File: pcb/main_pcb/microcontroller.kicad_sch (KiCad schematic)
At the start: 20 parts

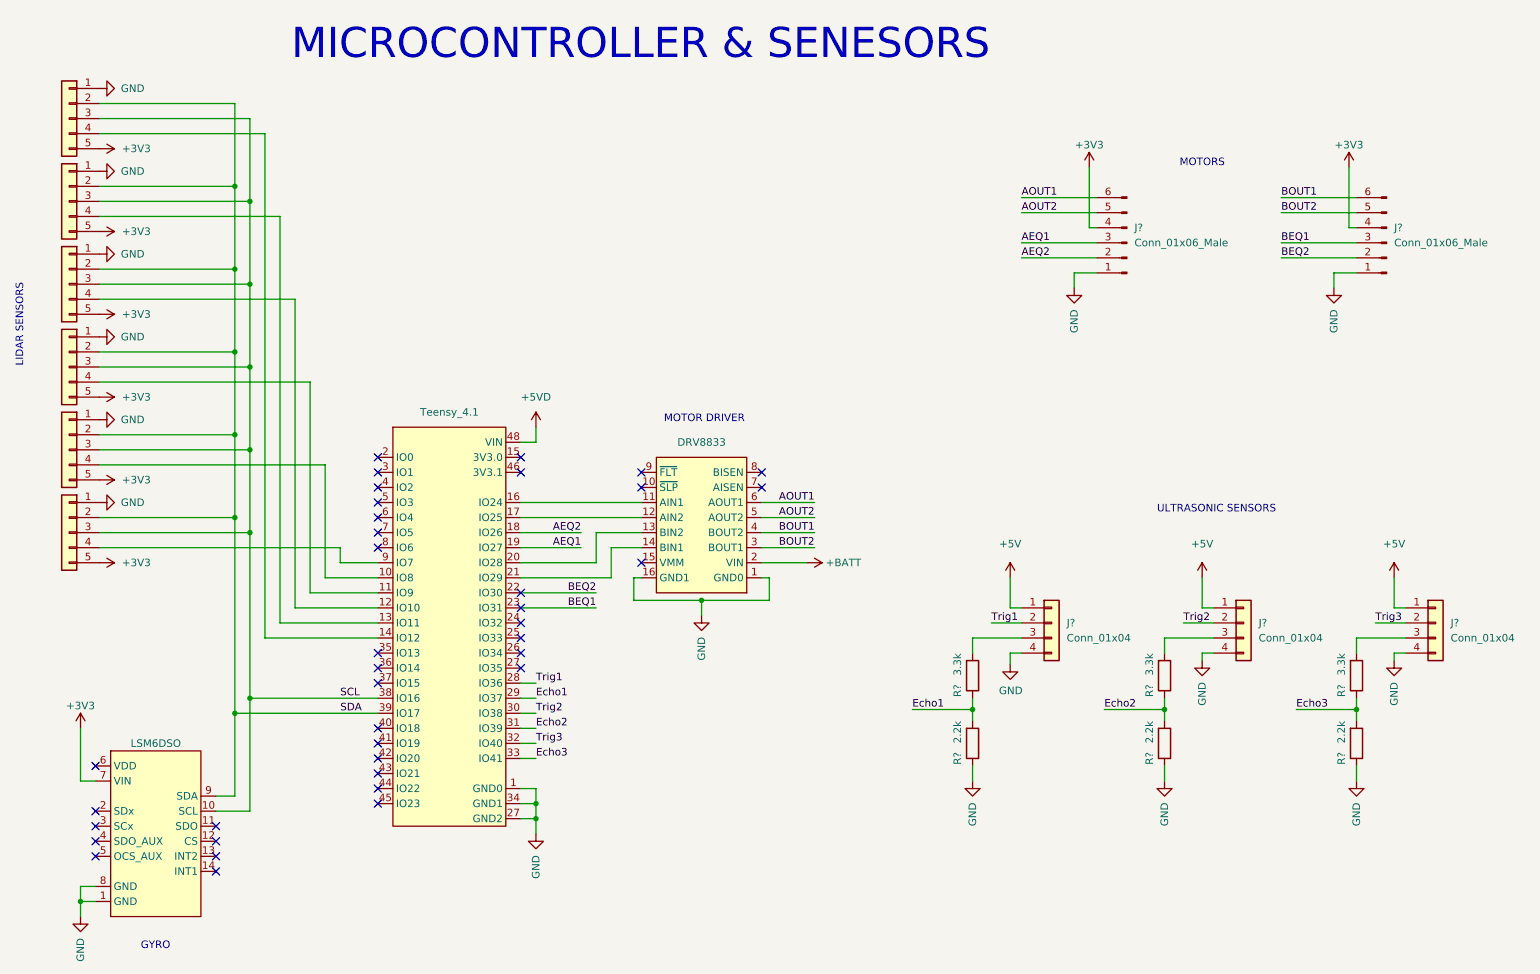
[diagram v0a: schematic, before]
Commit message: Annotate & begin footprint assignment
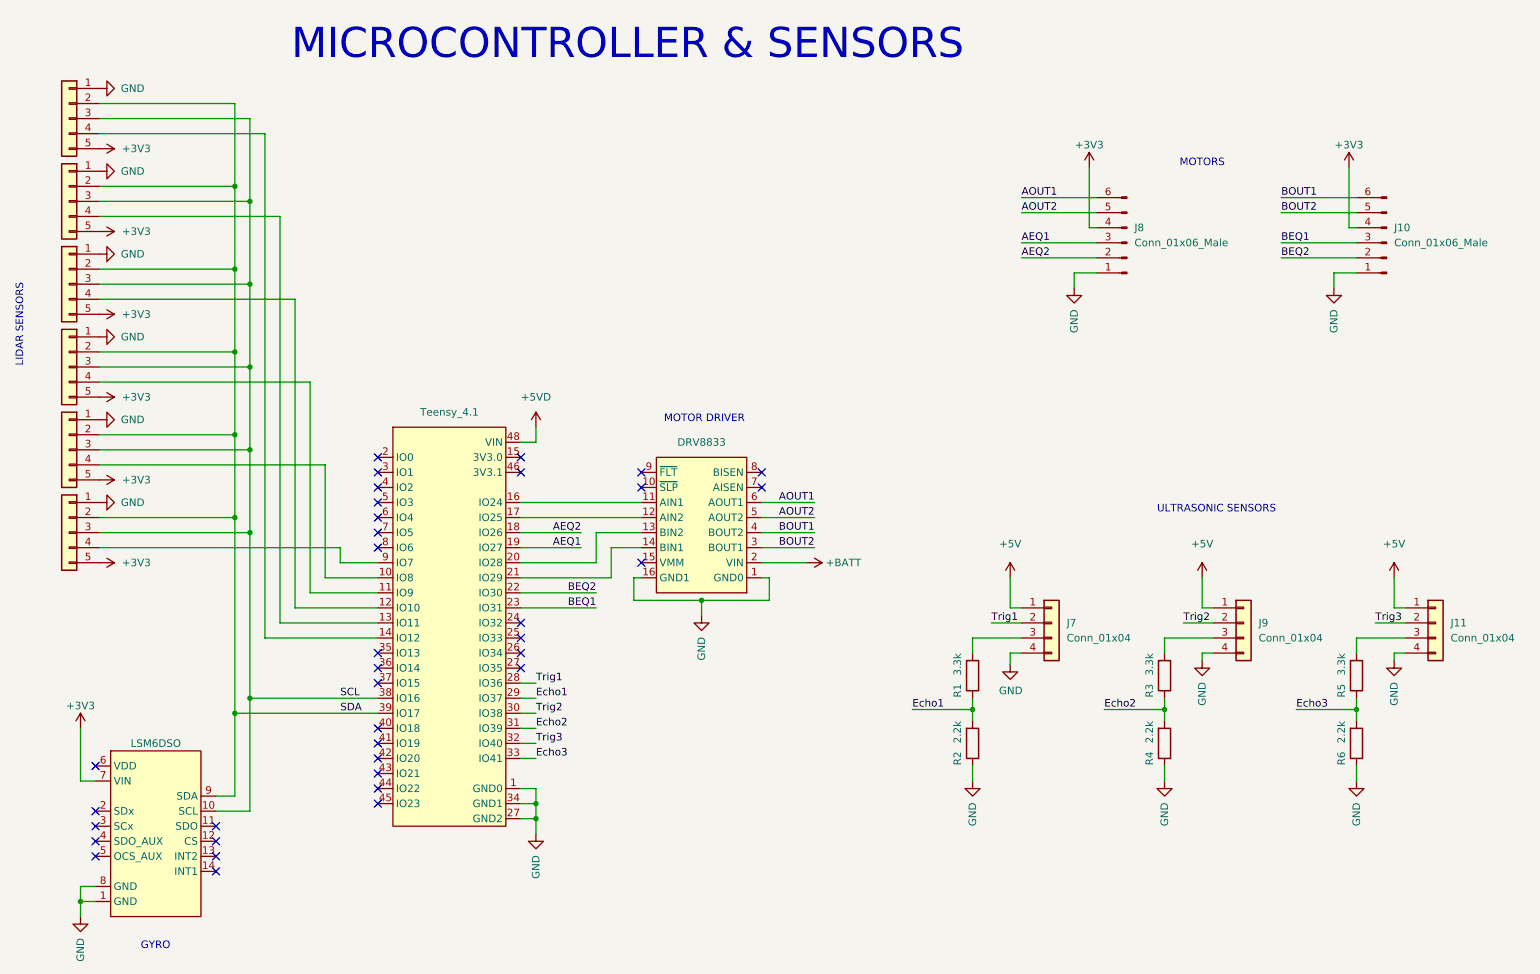
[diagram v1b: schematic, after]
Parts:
- removed J? (x5): Conn_01x04, symbol Connector_Generic:Conn_01x05
- added J2, J3, J4, J5, J6: Conn_01x05, Connector_JST:JST_XH_B5B-XH-A_1x05_P2.50mm_Vertical, symbol Connector_Generic:Conn_01x05
- J1: renamed from J?; value Conn_01x04 -> Conn_01x05; footprint (none) -> Connector_JST:JST_XH_B5B-XH-A_1x05_P2.50mm_Vertical
- J10, J8: renamed from J?; footprint (none) -> Connector_JST:JST_XH_B6B-XH-A_1x06_P2.50mm_Vertical
- J11, J7, J9: renamed from J?; footprint (none) -> Connector_JST:JST_XH_B4B-XH-A_1x04_P2.50mm_Vertical
- R1, R2, R3, R4, R5, R6: renamed from R?; footprint (none) -> Resistor_SMD:R_0603_1608Metric_Pad0.98x0.95mm_HandSolder
- gave numbers to parts that had none: 3
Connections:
- net +3V3: now also J2.5 (Pin_5), J3.5 (Pin_5), J4.5 (Pin_5), J5.5 (Pin_5), J6.5 (Pin_5)
- net GND: now also J2.1 (Pin_1), J3.1 (Pin_1), J4.1 (Pin_1), J5.1 (Pin_1), J6.1 (Pin_1)
- net SCL: now also J2.3 (Pin_3), J3.3 (Pin_3), J4.3 (Pin_3), J5.3 (Pin_3), J6.3 (Pin_3)
- net SDA: now also J2.2 (Pin_2), J3.2 (Pin_2), J4.2 (Pin_2), J5.2 (Pin_2), J6.2 (Pin_2)
- net at U2.10 (IO8): now also J5.4 (Pin_4)
- net at U2.11 (IO9): now also J4.4 (Pin_4)
- net at U2.13 (IO11): now also J2.4 (Pin_4)
- net at U2.12 (IO10): now also J3.4 (Pin_4)
- net at U2.9 (IO7): now also J6.4 (Pin_4)
- no-connect marks 38 -> 36
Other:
- note added: "MICROCONTROLLER & SENSORS"
- note removed: "MICROCONTROLLER & SENESORS"

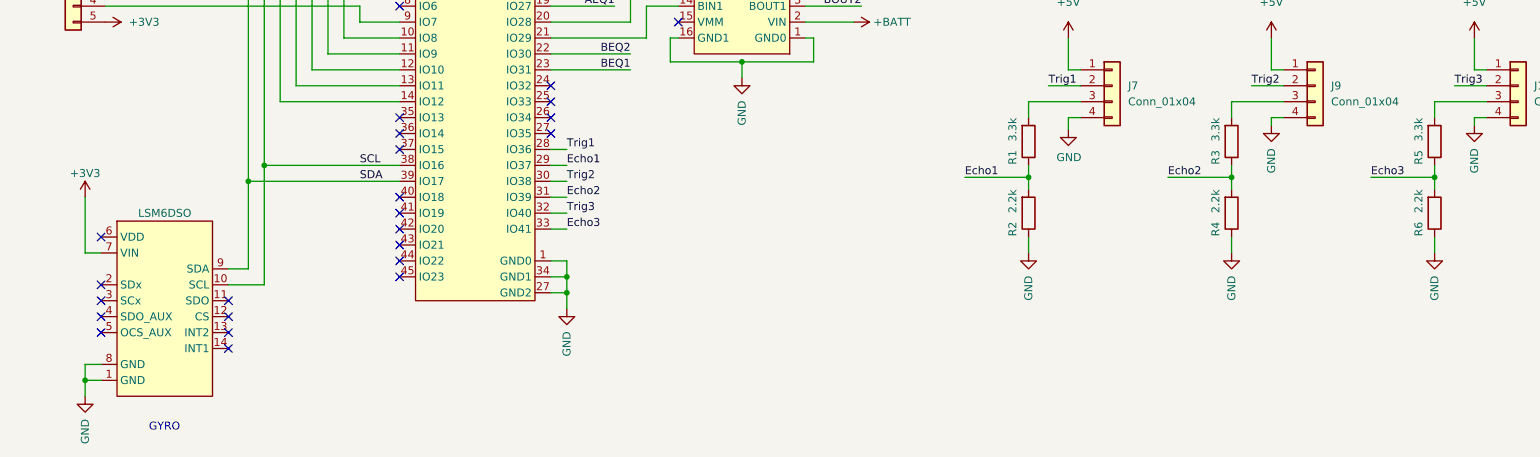
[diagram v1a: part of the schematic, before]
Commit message: Create footprints for carriers; complete footprint assignment
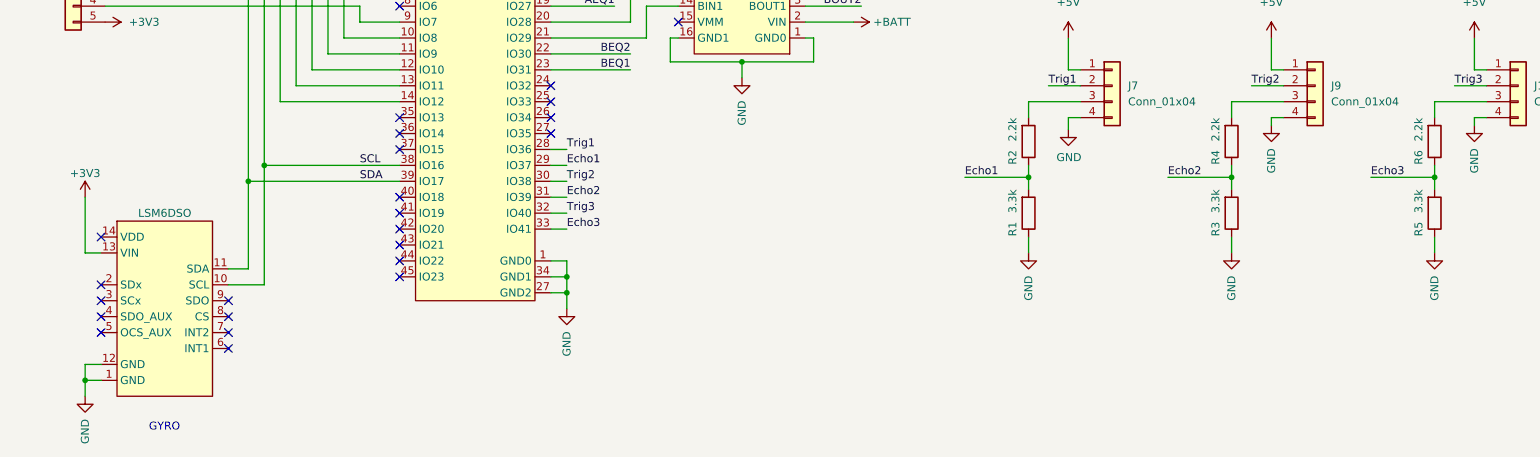
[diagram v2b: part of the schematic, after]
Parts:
- U1: footprint (none) -> custom_footprints:SENS_LSM6DSO_Pololu_2798
- U2: footprint (none) -> custom_footprints:MCU_TEENSY41_PJRC
- U3: footprint (none) -> custom_footprints:DRV_DRV8833_Pololu_2130
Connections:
- net +3V3: now also U1.13 (VIN); no longer U1.7 (VIN)
- net Echo1: now also R1.2, R2.1; no longer R1.1, R2.2
- net Echo2: now also R3.2, R4.1; no longer R3.1, R4.2
- net Echo3: now also R5.2, R6.1; no longer R5.1, R6.2
- net GND: now also R1.1, R3.1, R5.1, U1.12 (GND); no longer R2.1, R4.1, R6.1, U1.8 (GND)
- net SDA: now also U1.11 (SDA); no longer U1.9 (SDA)
- net at J7.3 (Pin_3): now also R2.2; no longer R1.2
- net at J9.3 (Pin_3): now also R4.2; no longer R3.2
- net at J11.3 (Pin_3): now also R6.2; no longer R5.2
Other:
- moved on the sheet: R1, R2, R3, R4, R5, R6
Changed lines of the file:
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@@
     (pin "1")
   )
-  (symbol (lib_id "Device:R") (at 182.88 130.81 0) (mirror x) (unit 1)
-    (in_bom yes) (on_board yes)
-    (property "Reference" "R1" (id 0) (at 180.34 133.35 90))
-    (property "Value" "3.3k" (id 1) (at 180.34 128.905 90))
-    (property "Footprint" "Resistor_SMD:R_0603_1608Metric_Pad0.98x0.95mm_HandSolder" (id 2) (at 181.102 130.81 90)
-      (effects (font (size 1.27 1.27)) hide)
-    )
-    (property "Datasheet" "~" (id 3) (at 182.88 130.81 0)
-      (effects (font (size 1.27 1.27)) hide)
-    )
-    (pin "1")
-    (pin "2")
-  )
-  (symbol (lib_id "Device:R") (at 215.265 130.81 0) (mirror x) (unit 1)
-    (in_bom yes) (on_board yes)
-    (property "Reference" "R3" (id 0) (at 212.725 133.35 90))
-    (property "Value" "3.3k" (id 1) (at 212.725 128.905 90))
-    (property "Footprint" "Resistor_SMD:R_0603_1608Metric_Pad0.98x0.95mm_HandSolder" (id 2) (at 213.487 130.81 90)
-      (effects (font (size 1.27 1.27)) hide)
-    )
-    (property "Datasheet" "~" (id 3) (at 215.265 130.81 0)
+  (symbol (lib_id "Device:R") (at 182.88 142.24 0) (mirror x) (unit 1)
+    (in_bom yes) (on_board yes)
+    (property "Reference" "R1" (id 0) (at 180.34 144.78 90))
+    (property "Value" "3.3k" (id 1) (at 180.34 140.335 90))
+    (property "Footprint" "Resistor_SMD:R_0603_1608Metric_Pad0.98x0.95mm_HandSolder" (id 2) (at 181.102 142.24 90)
+      (effects (font (size 1.27 1.27)) hide)
+    )
+    (property "Datasheet" "~" (id 3) (at 182.88 142.24 0)
+      (effects (font (size 1.27 1.27)) hide)
+    )
+    (pin "1")
+    (pin "2")
+  )
+  (symbol (lib_id "Device:R") (at 215.265 142.24 0) (mirror x) (unit 1)
+    (in_bom yes) (on_board yes)
+    (property "Reference" "R3" (id 0) (at 212.725 144.78 90))
+    (property "Value" "3.3k" (id 1) (at 212.725 140.335 90))
+    (property "Footprint" "Resistor_SMD:R_0603_1608Metric_Pad0.98x0.95mm_HandSolder" (id 2) (at 213.487 142.24 90)
+      (effects (font (size 1.27 1.27)) hide)
+    )
+    (property "Datasheet" "~" (id 3) (at 215.265 142.24 0)
       (effects (font (size 1.27 1.27)) hide)
     )
@@
     )
     (property "Value" "LSM6DSO" (id 1) (at 45.085 142.24 0))
-    (property "Footprint" "" (id 2) (at 41.275 152.4 0)
+    (property "Footprint" "custom_footprints:SENS_LSM6DSO_Pololu_2798" (id 2) (at 41.275 152.4 0)
       (effects (font (size 1.27 1.27)) hide)
     )
@@
     )
     (property "Value" "DRV8833" (id 1) (at 137.16 91.44 0))
-    (property "Footprint" "" (id 2) (at 142.24 110.49 0)
+    (property "Footprint" "custom_footprints:DRV_DRV8833_Pololu_2130" (id 2) (at 142.24 110.49 0)
       (effects (font (size 1.27 1.27)) hide)
     )
@@
     )
     (property "Value" "Teensy_4.1" (id 1) (at 94.615 86.36 0))
-    (property "Footprint" "" (id 2) (at 72.39 114.3 0)
+    (property "Footprint" "custom_footprints:MCU_TEENSY41_PJRC" (id 2) (at 72.39 114.3 0)
       (effects (font (size 1.27 1.27)) hide)
     )
@@
     (pin "1")
   )
-  (symbol (lib_id "Device:R") (at 247.65 130.81 0) (mirror x) (unit 1)
-    (in_bom yes) (on_board yes)
-    (property "Reference" "R5" (id 0) (at 245.11 133.35 90))
-    (property "Value" "3.3k" (id 1) (at 245.11 128.905 90))
-    (property "Footprint" "Resistor_SMD:R_0603_1608Metric_Pad0.98x0.95mm_HandSolder" (id 2) (at 245.872 130.81 90)
-      (effects (font (size 1.27 1.27)) hide)
-    )
-    (property "Datasheet" "~" (id 3) (at 247.65 130.81 0)
+  (symbol (lib_id "Device:R") (at 247.65 142.24 0) (mirror x) (unit 1)
+    (in_bom yes) (on_board yes)
+    (property "Reference" "R5" (id 0) (at 245.11 144.78 90))
+    (property "Value" "3.3k" (id 1) (at 245.11 140.335 90))
+    (property "Footprint" "Resistor_SMD:R_0603_1608Metric_Pad0.98x0.95mm_HandSolder" (id 2) (at 245.872 142.24 90)
+      (effects (font (size 1.27 1.27)) hide)
+    )
+    (property "Datasheet" "~" (id 3) (at 247.65 142.24 0)
       (effects (font (size 1.27 1.27)) hide)
     )
@@
     (pin "1")
   )
-  (symbol (lib_id "Device:R") (at 247.65 142.24 0) (mirror x) (unit 1)
-    (in_bom yes) (on_board yes)
-    (property "Reference" "R6" (id 0) (at 245.11 144.78 90))
-    (property "Value" "2.2k" (id 1) (at 245.11 140.335 90))
-    (property "Footprint" "Resistor_SMD:R_0603_1608Metric_Pad0.98x0.95mm_HandSolder" (id 2) (at 245.872 142.24 90)
-      (effects (font (size 1.27 1.27)) hide)
-    )
-    (property "Datasheet" "~" (id 3) (at 247.65 142.24 0)
+  (symbol (lib_id "Device:R") (at 247.65 130.81 0) (mirror x) (unit 1)
+    (in_bom yes) (on_board yes)
+    (property "Reference" "R6" (id 0) (at 245.11 133.35 90))
+    (property "Value" "2.2k" (id 1) (at 245.11 128.905 90))
+    (property "Footprint" "Resistor_SMD:R_0603_1608Metric_Pad0.98x0.95mm_HandSolder" (id 2) (at 245.872 130.81 90)
+      (effects (font (size 1.27 1.27)) hide)
+    )
+    (property "Datasheet" "~" (id 3) (at 247.65 130.81 0)
       (effects (font (size 1.27 1.27)) hide)
     )
@@
     (pin "4")
   )
-  (symbol (lib_id "Device:R") (at 215.265 142.24 0) (mirror x) (unit 1)
-    (in_bom yes) (on_board yes)
-    (property "Reference" "R4" (id 0) (at 212.725 144.78 90))
-    (property "Value" "2.2k" (id 1) (at 212.725 140.335 90))
-    (property "Footprint" "Resistor_SMD:R_0603_1608Metric_Pad0.98x0.95mm_HandSolder" (id 2) (at 213.487 142.24 90)
-      (effects (font (size 1.27 1.27)) hide)
-    )
-    (property "Datasheet" "~" (id 3) (at 215.265 142.24 0)
+  (symbol (lib_id "Device:R") (at 215.265 130.81 0) (mirror x) (unit 1)
+    (in_bom yes) (on_board yes)
+    (property "Reference" "R4" (id 0) (at 212.725 133.35 90))
+    (property "Value" "2.2k" (id 1) (at 212.725 128.905 90))
+    (property "Footprint" "Resistor_SMD:R_0603_1608Metric_Pad0.98x0.95mm_HandSolder" (id 2) (at 213.487 130.81 90)
+      (effects (font (size 1.27 1.27)) hide)
+    )
+    (property "Datasheet" "~" (id 3) (at 215.265 130.81 0)
       (effects (font (size 1.27 1.27)) hide)
     )
@@
     (pin "1")
   )
-  (symbol (lib_id "Device:R") (at 182.88 142.24 0) (mirror x) (unit 1)
-    (in_bom yes) (on_board yes)
-    (property "Reference" "R2" (id 0) (at 180.34 144.78 90))
-    (property "Value" "2.2k" (id 1) (at 180.34 140.335 90))
-    (property "Footprint" "Resistor_SMD:R_0603_1608Metric_Pad0.98x0.95mm_HandSolder" (id 2) (at 181.102 142.24 90)
-      (effects (font (size 1.27 1.27)) hide)
-    )
-    (property "Datasheet" "~" (id 3) (at 182.88 142.24 0)
-      (effects (font (size 1.27 1.27)) hide)
-    )
+  (symbol (lib_id "Device:R") (at 182.88 130.81 0) (mirror x) (unit 1)
+    (in_bom yes) (on_board yes)
+    (property "Reference" "R2" (id 0) (at 180.34 133.35 90))
+    (property "Value" "2.2k" (id 1) (at 180.34 128.905 90))
+    (property "Footprint" "Resistor_SMD:R_0603_1608Metric_Pad0.98x0.95mm_HandSolder" (id 2) (at 181.102 130.81 90)
+      (effects (font (size 1.27 1.27)) hide)
+    )
+    (property "Datasheet" "~" (id 3) (at 182.88 130.81 0)
+      (effects (font (size 1.27 1.27)) hide)
+    )
